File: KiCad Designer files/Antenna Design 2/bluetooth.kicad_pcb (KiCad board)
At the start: 32 copper layers, 47 x 37 mm, 56 parts, among them U1 Multi-protocol Bluetooth Low 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, U1 O, U10 O, U102 O, U11 O, U12 O, U13 O, U14 O, U15 O, U16 O, U17 O, U18 O, U19 O, U2 O, U20 O, U21 O, U23 O, U24 O, U25 O, U26 O, U27 O, U28 O, U29 O, U3 O, U30 O, U31 O, U32 O, U33 O, U4 O, U5 O, U6 O, U7 O, U8 O, U9 O

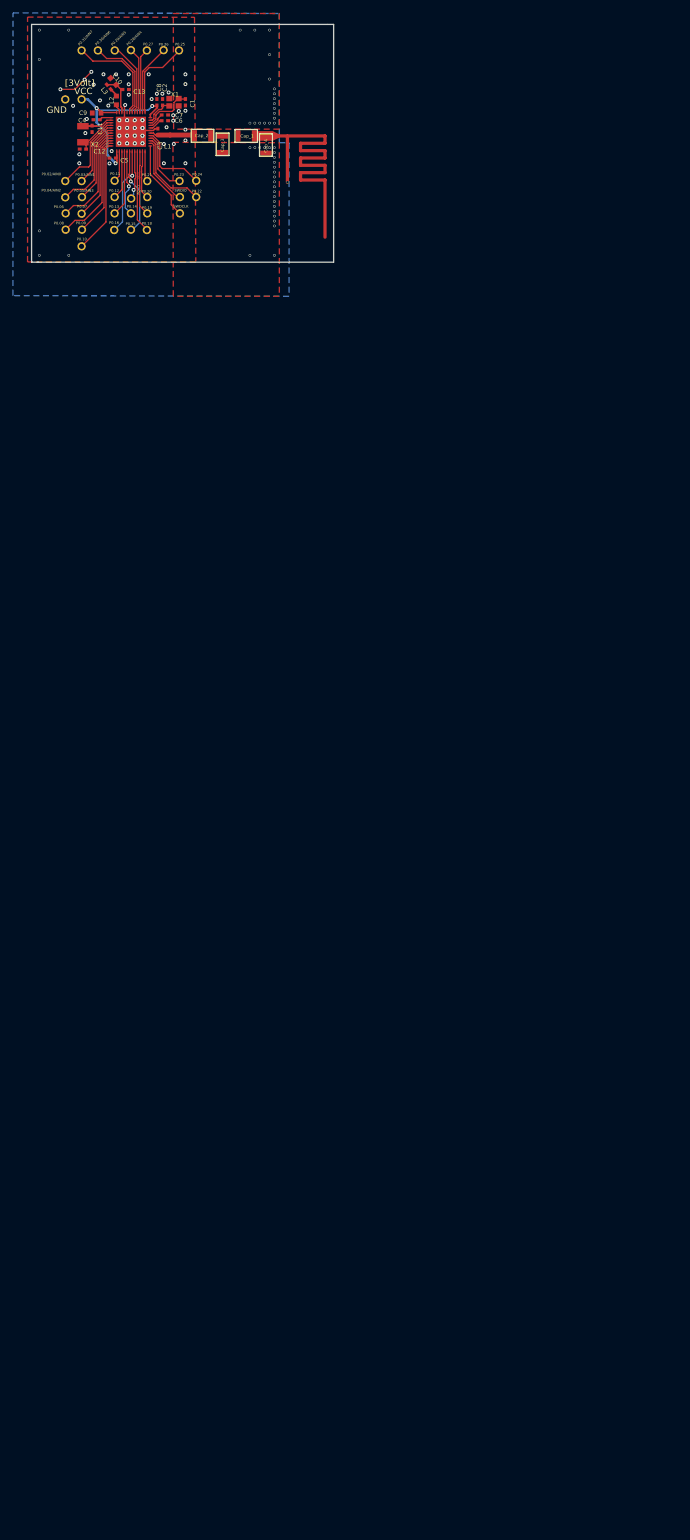
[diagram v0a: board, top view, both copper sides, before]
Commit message: changed pcb position to the center of the pcbnew
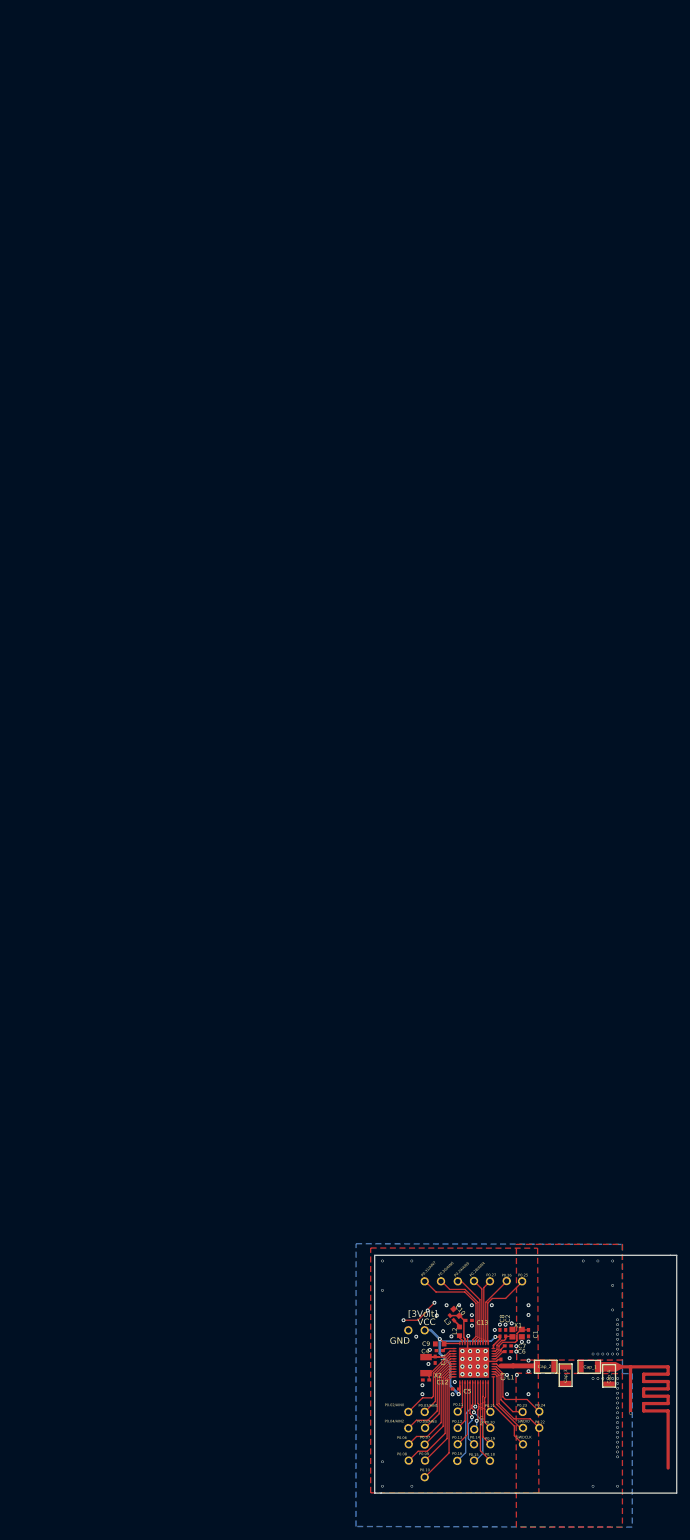
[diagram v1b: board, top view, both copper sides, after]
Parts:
- moved C1 198.8 mm to (146.0, 101.5)
- moved C10 198.8 mm to (134.8, 98.2)
- moved C12 198.8 mm to (130.0, 108.7)
- moved C13 198.8 mm to (136.7, 99.5)
- moved C2 198.8 mm to (142.4, 101.5)
- moved C5 198.8 mm to (134.7, 110.1)
- moved C7 198.8 mm to (142.8, 103.4)
- moved C8 198.8 mm to (141.5, 101.5)
- moved C9 198.8 mm to (132.2, 103.1)
- moved Cap_2 198.8 mm to (148.6, 106.7)
- moved Cap_3 198.8 mm to (151.8, 108.0)
- moved L2 198.8 mm to (135.2, 101.2)
- moved U1 198.8 mm to (145.0, 93.3)
- moved U102 198.8 mm to (140.1, 116.2)
- moved U11 198.8 mm to (135.0, 116.2)
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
